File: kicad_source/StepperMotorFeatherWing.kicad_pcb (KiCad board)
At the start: 2 copper layers, 100 x 60 mm, 80 parts, among them CN1 ADAFRUIT_FEATHER, P1 WR-TBL_691322310002, P10 CONN_01X04, P2 WR-TBL_691313710002, P3 CONN_01X04, P4 CONN_01X05, P5 CONN_01X04, P6 CONN_01X05, P7 CONN_01X04, P8 CONN_01X04, P9 CONN_01X04, Q1 IPD90P03P4L- 04, U1 TMC5130A-TA, U2 TMC5130A-TA, U9 IFX91041EJV

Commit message: generated pdf files
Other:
- board text added: "Copyright generationmake 2019 see full project documentation at https://github.com/generationmake/StepperMotorFeatherWing This documentation describes Open Hardware and is licensed under the CERN OHL v. 1.2. You may redistribute and modify this documentation under the terms of the CERN OHL v.1.2. (http://ohwr.org/cernohl). This documentation is distributed WITHOUT ANY EXPRESS OR IMPLIED WARRANTY,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"
- board text removed: "Copyright generationmake 2019 see full project documentation at http://arduhmi.generationmake.de This documentation describes Open Hardware and is licensed under the CERN OHL v. 1.2. You may redistribute and modify this documentation under the terms of the CERN OHL v.1.2. (http://ohwr.org/cernohl). This documentation is distributed WITHOUT ANY EXPRESS OR IMPLIED WARRANTY, INCLUDING OF MERCHANTABI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"

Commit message: added mounting instructions
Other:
- board text added: "4x for heatspreader"
- board text added: "8x"
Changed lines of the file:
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@@
   (general
     (thickness 1.6)
-    (drawings 42)
+    (drawings 69)
     (tracks 901)
     (zones 0)
@@
     (pad "" smd rect (at 2.8 -1.2625) (size 1.2 1.8) (layers F.Cu F.Paste F.Mask))
   )
+  (dimension 26.5 (width 0.15) (layer Eco1.User)
+    (gr_text "26,500 mm" (at 156.3 82.25 90) (layer Eco1.User)
+      (effects (font (size 1 1) (thickness 0.15)))
+    )
+    (feature1 (pts (xy 148 69) (xy 155.586421 69)))
+    (feature2 (pts (xy 148 95.5) (xy 155.586421 95.5)))
+    (crossbar (pts (xy 155 95.5) (xy 155 69)))
+    (arrow1a (pts (xy 155 69) (xy 155.586421 70.126504)))
+    (arrow1b (pts (xy 155 69) (xy 154.413579 70.126504)))
+    (arrow2a (pts (xy 155 95.5) (xy 155.586421 94.373496)))
+    (arrow2b (pts (xy 155 95.5) (xy 154.413579 94.373496)))
+  )
+  (gr_text "8x " (at 62.6 74.3 90) (layer Eco1.User)
+    (effects (font (size 1 1) (thickness 0.15)))
+  )
+  (dimension 3.2 (width 0.15) (layer Eco1.User)
+    (gr_text "3,200 mm" (at 62.6 69 90) (layer Eco1.User)
+      (effects (font (size 1 1) (thickness 0.15)))
+    )
+    (feature1 (pts (xy 54 67.4) (xy 61.886421 67.4)))
+    (feature2 (pts (xy 54 70.6) (xy 61.886421 70.6)))
+    (crossbar (pts (xy 61.3 70.6) (xy 61.3 67.4)))
+    (arrow1a (pts (xy 61.3 67.4) (xy 61.886421 68.526504)))
+    (arrow1b (pts (xy 61.3 67.4) (xy 60.713579 68.526504)))
+    (arrow2a (pts (xy 61.3 70.6) (xy 61.886421 69.473496)))
+    (arrow2b (pts (xy 61.3 70.6) (xy 60.713579 69.473496)))
+  )
+  (gr_line (start 133.5 93) (end 141 121) (layer Eco1.User) (width 0.15))
+  (gr_line (start 133.5 92) (end 141 71) (layer Eco1.User) (width 0.15))
+  (gr_line (start 133.5 92.5) (end 146 95) (layer Eco1.User) (width 0.15))
+  (gr_line (start 117.5 92.5) (end 102 95) (layer Eco1.User) (width 0.15))
+  (gr_text "4x for heatspreader" (at 125.5 92.5) (layer Eco1.User)
+    (effects (font (size 1 1) (thickness 0.15)))
+  )
+  (gr_line (start 100 95.5) (end 100 123) (layer Eco1.User) (width 0.15))
+  (gr_line (start 100 95.5) (end 148 95.5) (layer Eco1.User) (width 0.15))
+  (dimension 27.5 (width 0.15) (layer Eco1.User)
+    (gr_text "27,500 mm" (at 156.3 109.25 90) (layer Eco1.User)
+      (effects (font (size 1 1) (thickness 0.15)))
+    )
+    (feature1 (pts (xy 148 95.5) (xy 155.586421 95.5)))
+    (feature2 (pts (xy 148 123) (xy 155.586421 123)))
+    (crossbar (pts (xy 155 123) (xy 155 95.5)))
+    (arrow1a (pts (xy 155 95.5) (xy 155.586421 96.626504)))
+    (arrow1b (pts (xy 155 95.5) (xy 154.413579 96.626504)))
+    (arrow2a (pts (xy 155 123) (xy 155.586421 121.873496)))
+    (arrow2b (pts (xy 155 123) (xy 154.413579 121.873496)))
+  )
+  (dimension 3 (width 0.15) (layer Eco1.User)
+    (gr_text "3,000 mm" (at 160.3 124.5 90) (layer Eco1.User)
+      (effects (font (size 1 1) (thickness 0.15)))
+    )
+    (feature1 (pts (xy 148 123) (xy 159.586421 123)))
+    (feature2 (pts (xy 148 126) (xy 159.586421 126)))
+    (crossbar (pts (xy 159 126) (xy 159 123)))
+    (arrow1a (pts (xy 159 123) (xy 159.586421 124.126504)))
+    (arrow1b (pts (xy 159 123) (xy 158.413579 124.126504)))
+    (arrow2a (pts (xy 159 126) (xy 159.586421 124.873496)))
+    (arrow2b (pts (xy 159 126) (xy 158.413579 124.873496)))
+  )
+  (dimension 54 (width 0.15) (layer Eco1.User)
+    (gr_text "54,000 mm" (at 160.3 96 90) (layer Eco1.User)
+      (effects (font (size 1 1) (thickness 0.15)))
+    )
+    (feature1 (pts (xy 148 69) (xy 159.586421 69)))
+    (feature2 (pts (xy 148 123) (xy 159.586421 123)))
+    (crossbar (pts (xy 159 123) (xy 159 69)))
+    (arrow1a (pts (xy 159 69) (xy 159.586421 70.126504)))
+    (arrow1b (pts (xy 159 69) (xy 158.413579 70.126504)))
+    (arrow2a (pts (xy 159 123) (xy 159.586421 121.873496)))
+    (arrow2b (pts (xy 159 123) (xy 158.413579 121.873496)))
+  )
+  (dimension 42 (width 0.15) (layer Eco1.User)
+    (gr_text "42,000 mm" (at 121 131.3) (layer Eco1.User)
+      (effects (font (size 1 1) (thickness 0.15)))
+    )
+    (feature1 (pts (xy 100 123) (xy 100 130.586421)))
+    (feature2 (pts (xy 142 123) (xy 142 130.586421)))
+    (crossbar (pts (xy 142 130) (xy 100 130)))
+    (arrow1a (pts (xy 100 130) (xy 101.126504 129.413579)))
+    (arrow1b (pts (xy 100 130) (xy 101.126504 130.586421)))
+    (arrow2a (pts (xy 142 130) (xy 140.873496 129.413579)))
+    (arrow2b (pts (xy 142 130) (xy 140.873496 130.586421)))
+  )
+  (dimension 6 (width 0.15) (layer Eco1.User)
+    (gr_text "6,000 mm" (at 145 131.3) (layer Eco1.User)
+      (effects (font (size 1 1) (thickness 0.15)))
+    )
+    (feature1 (pts (xy 148 123) (xy 148 130.586421)))
+    (feature2 (pts (xy 142 123) (xy 142 130.586421)))
+    (crossbar (pts (xy 142 130) (xy 148 130)))
+    (arrow1a (pts (xy 148 130) (xy 146.873496 130.586421)))
+    (arrow1b (pts (xy 148 130) (xy 146.873496 129.413579)))
+    (arrow2a (pts (xy 142 130) (xy 143.126504 130.586421)))
+    (arrow2b (pts (xy 142 130) (xy 143.126504 129.413579)))
+  )
+  (dimension 3 (width 0.15) (layer Eco1.User)
+    (gr_text "3,000 mm" (at 52.5 134.8) (layer Eco1.User)
+      (effects (font (size 1 1) (thickness 0.15)))
+    )
+    (feature1 (pts (xy 54 123) (xy 54 134.086421)))
+    (feature2 (pts (xy 51 123) (xy 51 134.086421)))
+    (crossbar (pts (xy 51 133.5) (xy 54 133.5)))
+    (arrow1a (pts (xy 54 133.5) (xy 52.873496 134.086421)))
+    (arrow1b (pts (xy 54 133.5) (xy 52.873496 132.913579)))
+    (arrow2a (pts (xy 51 133.5) (xy 52.126504 134.086421)))
+    (arrow2b (pts (xy 51 133.5) (xy 52.126504 132.913579)))
+  )
+  (dimension 94 (width 0.15) (layer Eco1.User)
+    (gr_text "94,000 mm" (at 101 134.8) (layer Eco1.User)
+      (effects (font (size 1 1) (thickness 0.15)))
+    )
+    (feature1 (pts (xy 148 123) (xy 148 134.086421)))
+    (feature2 (pts (xy 54 123) (xy 54 134.086421)))
+    (crossbar (pts (xy 54 133.5) (xy 148 133.5)))
+    (arrow1a (pts (xy 148 133.5) (xy 146.873496 134.086421)))
+    (arrow1b (pts (xy 148 133.5) (xy 146.873496 132.913579)))
+    (arrow2a (pts (xy 54 133.5) (xy 55.126504 134.086421)))
+    (arrow2b (pts (xy 54 133.5) (xy 55.126504 132.913579)))
+  )
+  (dimension 3 (width 0.15) (layer Eco1.User)
+    (gr_text "3,000 mm" (at 45.2 124.5 90) (layer Eco1.User)
+      (effects (font (size 1 1) (thickness 0.15)))
+    )
+    (feature1 (pts (xy 54 123) (xy 45.913579 123)))
+    (feature2 (pts (xy 54 126) (xy 45.913579 126)))
+    (crossbar (pts (xy 46.5 126) (xy 46.5 123)))
+    (arrow1a (pts (xy 46.5 123) (xy 47.086421 124.126504)))
+    (arrow1b (pts (xy 46.5 123) (xy 45.913579 124.126504)))
+    (arrow2a (pts (xy 46.5 126) (xy 47.086421 124.873496)))
+    (arrow2b (pts (xy 46.5 126) (xy 45.913579 124.873496)))
+  )
+  (dimension 54 (width 0.15) (layer Eco1.User)
+    (gr_text "54,000 mm" (at 45.2 96 90) (layer Eco1.User)
+      (effects (font (size 1 1) (thickness 0.15)))
+    )
+    (feature1 (pts (xy 54 69) (xy 45.913579 69)))
+    (feature2 (pts (xy 54 123) (xy 45.913579 123)))
+    (crossbar (pts (xy 46.5 123) (xy 46.5 69)))
+    (arrow1a (pts (xy 46.5 69) (xy 47.086421 70.126504)))
+    (arrow1b (pts (xy 46.5 69) (xy 45.913579 70.126504)))
+    (arrow2a (pts (xy 46.5 123) (xy 47.086421 121.873496)))
+    (arrow2b (pts (xy 46.5 123) (xy 45.913579 121.873496)))
+  )
+  (gr_circle (center 142 123) (end 143.6 123) (layer Eco1.User) (width 0.15))
+  (gr_circle (center 148 123) (end 149.6 123) (layer Eco1.User) (width 0.15))
+  (gr_circle (center 148 95.5) (end 149.6 95.5) (layer Eco1.User) (width 0.15))
+  (gr_circle (center 148 69) (end 149.6 69) (layer Eco1.User) (width 0.15))
+  (gr_circle (center 142 69) (end 143.6 69) (layer Eco1.User) (width 0.15))
+  (gr_circle (center 100 95.5) (end 101.6 95.5) (layer Eco1.User) (width 0.15))
+  (gr_circle (center 54 123) (end 55.6 123) (layer Eco1.User) (width 0.15))
+  (gr_circle (center 54 69) (end 55.6 69) (layer Eco1.User) (width 0.15))
   (dimension 100 (width 0.15) (layer Cmts.User)
     (gr_text "100,000 mm" (at 101 138.8) (layer Cmts.User)

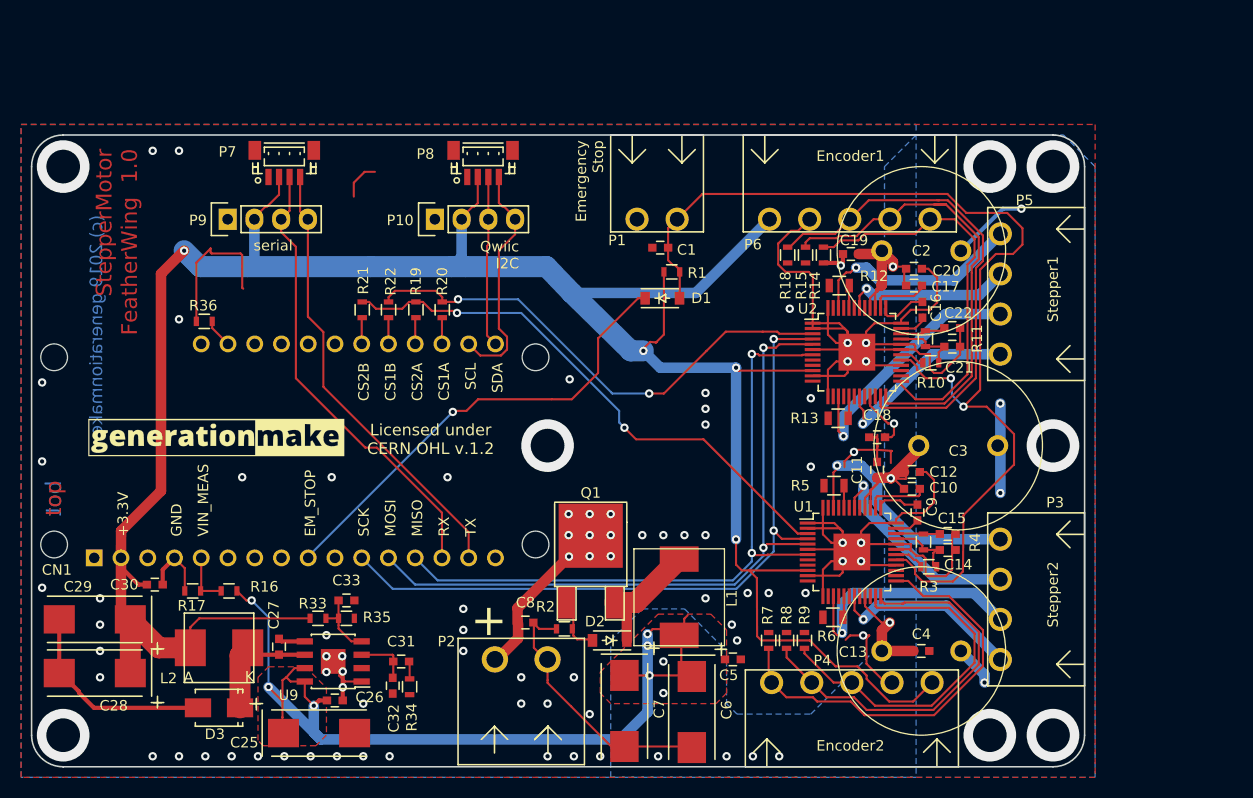
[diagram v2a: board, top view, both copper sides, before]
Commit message: added most missing 3d models, changed mounting holes to parts and generated step model
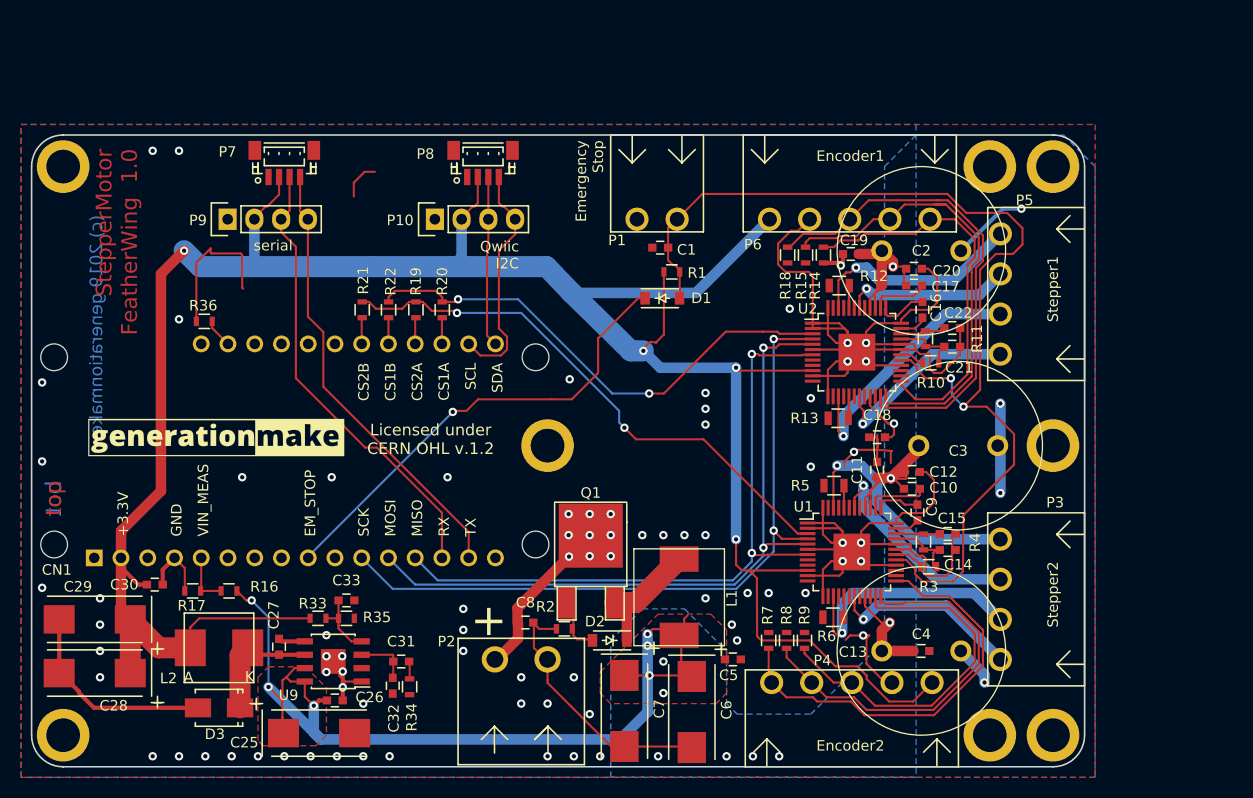
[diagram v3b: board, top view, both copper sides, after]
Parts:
- added MECH1: MHP_3.2_5.0, MECH_mounting_holes:MHP_3.2_5.0, F.Cu at (54.0, 69.0)
- added MECH2: MHP_3.2_5.0, MECH_mounting_holes:MHP_3.2_5.0, F.Cu at (54.0, 123.0)
- added MECH3: MHP_3.2_5.0, MECH_mounting_holes:MHP_3.2_5.0, F.Cu at (148.0, 69.0)
- added MECH4: MHP_3.2_5.0, MECH_mounting_holes:MHP_3.2_5.0, F.Cu at (148.0, 123.0)
- added MECH5: MHP_3.2_5.0, MECH_mounting_holes:MHP_3.2_5.0, F.Cu at (100.0, 95.5)
- added MECH6: MHP_3.2_5.0, MECH_mounting_holes:MHP_3.2_5.0, F.Cu at (142.0, 69.0)
- added MECH7: MHP_3.2_5.0, MECH_mounting_holes:MHP_3.2_5.0, F.Cu at (142.0, 123.0)
- added MECH8: MHP_3.2_5.0, MECH_mounting_holes:MHP_3.2_5.0, F.Cu at (148.0, 95.5)
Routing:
- net (no net): vias 8 -> 0

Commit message: added external supply for +5V for TMC5130
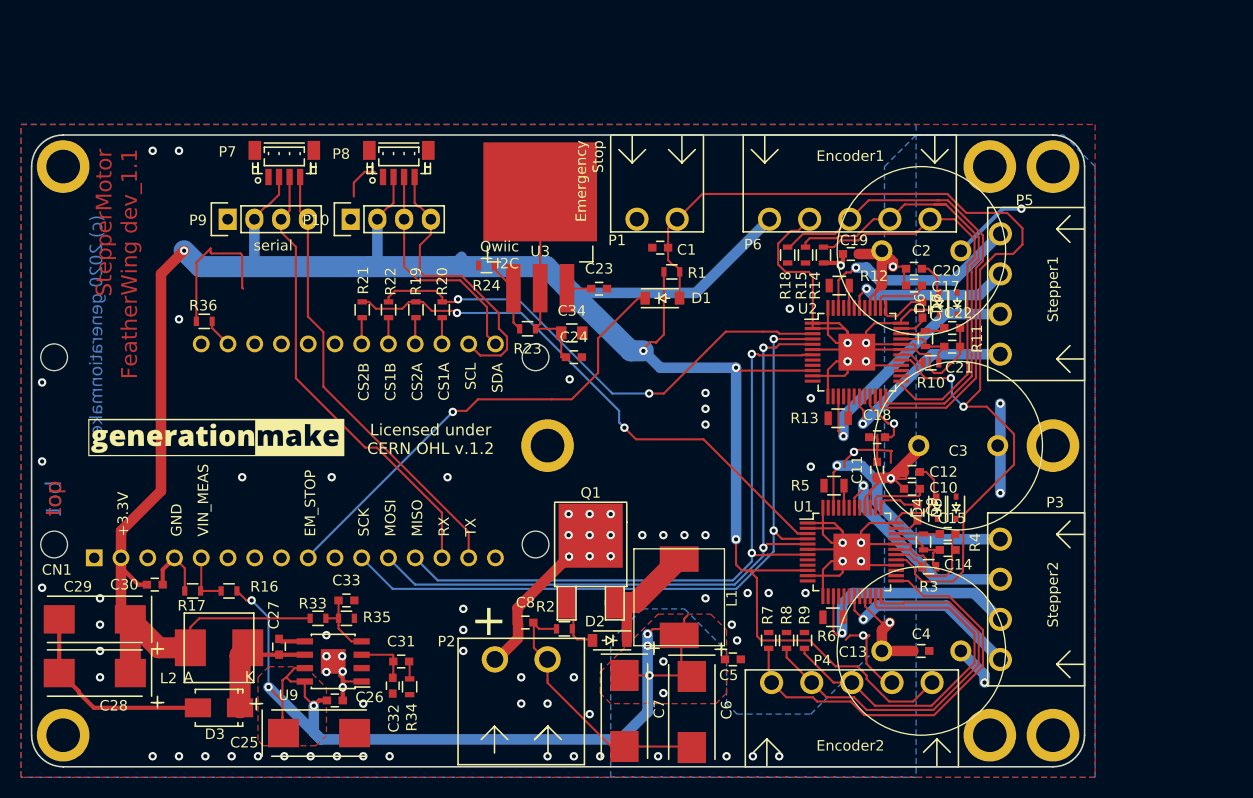
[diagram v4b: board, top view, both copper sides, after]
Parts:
- added C23: 100nF, capacitors:C_0603, F.Cu at (104.9, 80.6)
- added C24: 100nF, capacitors:C_0603, F.Cu at (102.5, 87.1)
- added C34: 10uF, capacitors:C_0805, F.Cu at (102.3, 84.8)
- added D4: BAT54HT1G, diodes:SOD-323, F.Cu at (137.0, 101.4)
- added D5: BAS16HT3G, diodes:SOD-323, F.Cu at (138.8, 101.4)
- added D6: BAT54HT1G, diodes:SOD-323, F.Cu at (137.2, 82.0)
- added D7: BAS16HT3G, diodes:SOD-323, F.Cu at (138.9, 82.0)
- added R23: 121, resistors:R_0603, F.Cu at (98.1, 84.4)
- added R24: 360, resistors:R_0603, F.Cu at (94.2, 78.4)
- added U3: LT1085, SOT_TO:TO-263-3Lead, F.Cu at (99.3, 80.5)
- R11, R4: value 2R2 -> DNI
- moved P10 8.00 mm to (81.3, 74.0)
- moved P8 8.00 mm to (85.9, 68.7)
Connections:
- net Net-(C15-Pad1) renamed /MotorDriver2/U2_VCC
- net Net-(C22-Pad1) renamed /MotorDriver1/U2_VCC
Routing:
- net +5V: track 0.00 -> 18.6 mm
- net Net-(R23-Pad2): track 0.00 -> 6.99 mm
- net I2C_SDA: track 16.2 -> 21.8 mm
- net I2C_SCL: track 22.4 -> 27.4 mm
- net VIN: track 143.5 -> 145.9 mm
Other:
- board text added: "(c) 2020 generationmake"
- board text added: "Copyright generationmake 2020 see full project documentation at https://github.com/generationmake/StepperMotorFeatherWing This documentation describes Open Hardware and is licensed under the CERN OHL v. 1.2. You may redistribute and modify this documentation under the terms of the CERN OHL v.1.2. (http://ohwr.org/cernohl). This documentation is distributed WITHOUT ANY EXPRESS OR IMPLIED WARRANTY,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"
- board text added: "StepperMotor FeatherWing dev_1.1"
- board text removed: "(c) 2019 generationmake"
- board text removed: "Copyright generationmake 2019 see full project documentation at https://github.com/generationmake/StepperMotorFeatherWing This documentation describes Open Hardware and is licensed under the CERN OHL v. 1.2. You may redistribute and modify this documentation under the terms of the CERN OHL v.1.2. (http://ohwr.org/cernohl). This documentation is distributed WITHOUT ANY EXPRESS OR IMPLIED WARRANTY,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"
- board text removed: "StepperMotor FeatherWing 1.0"

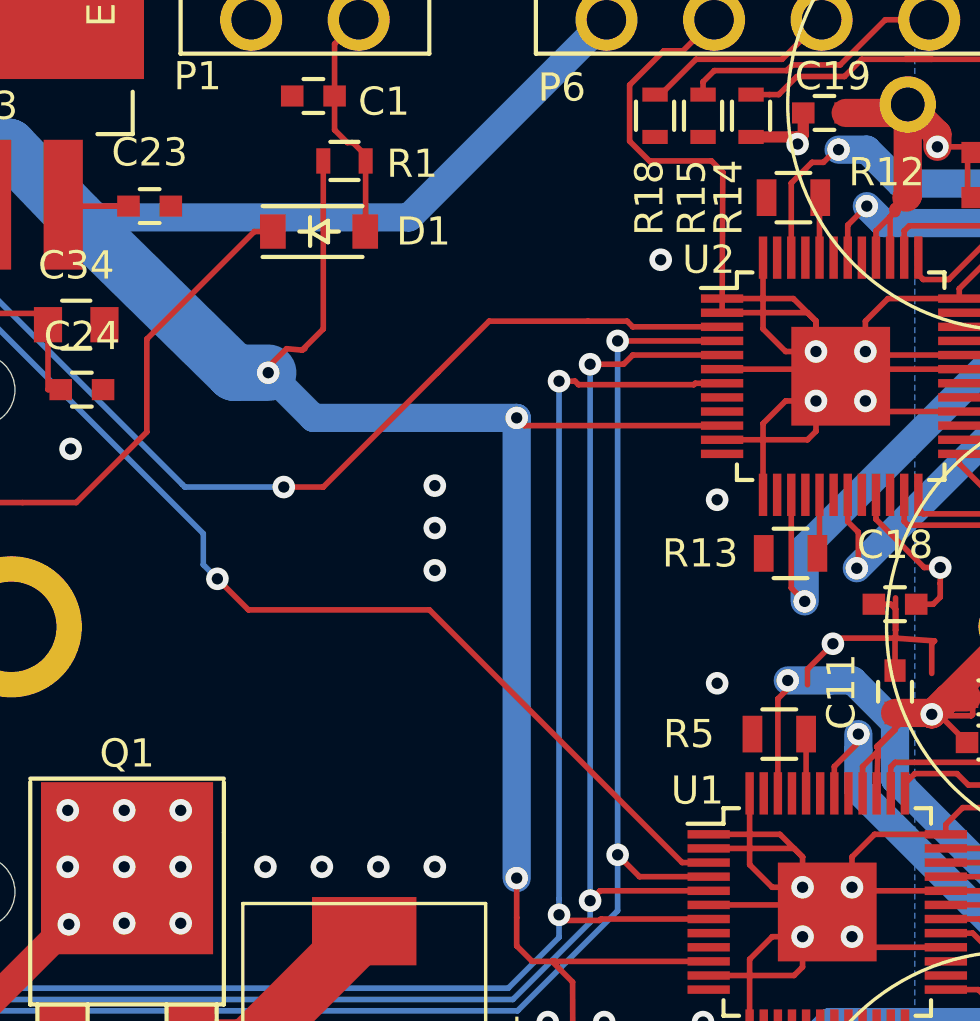
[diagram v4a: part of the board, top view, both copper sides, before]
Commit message: added clock generator as common clock for both stepper drivers
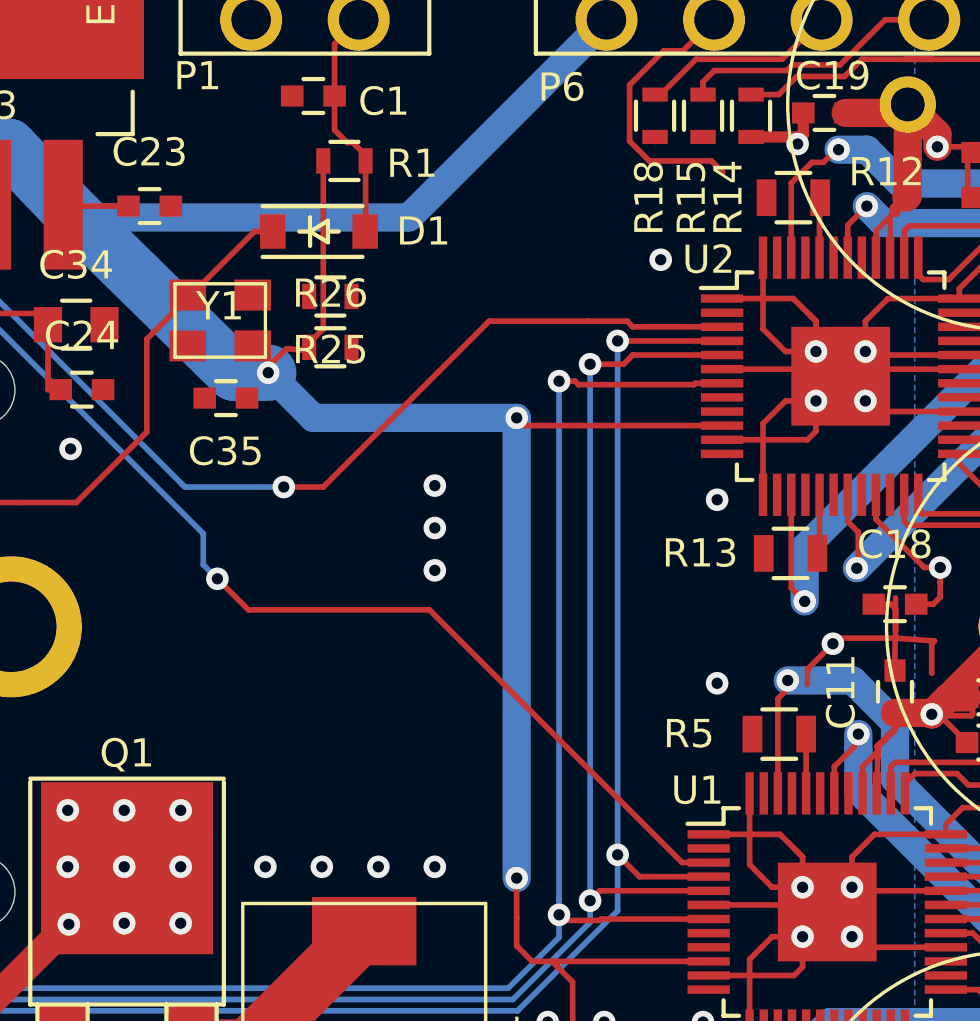
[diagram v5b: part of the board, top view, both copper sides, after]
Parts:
- added C35: 100nF, capacitors:C_0603, F.Cu at (107.6, 87.4)
- added R25: 33R, resistors:R_0603, F.Cu at (111.3, 83.8)
- added R26: DNI, resistors:R_0603, F.Cu at (111.3, 85.6)
- added Y1: oscillator, crystals:Crystal_SMD_3.2x2.5mm_4Pad, F.Cu at (107.4, 84.7)
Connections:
- U1 pad 2: GND -> CLK_16M
- U2 pad 2: GND -> CLK_16M
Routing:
- net GND: track 257.8 -> 246.8 mm
